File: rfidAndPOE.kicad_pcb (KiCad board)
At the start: 2 copper layers, 100 x 50 mm, 126 parts, among them J1 0813-1X1T-57-F, J2 SWD, J3 MCU Port B, J4 MCU Port C, P1 PoE-, P2 PoE+, P3 GND, P4 +5V, P5 +12V, P6 +3V3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

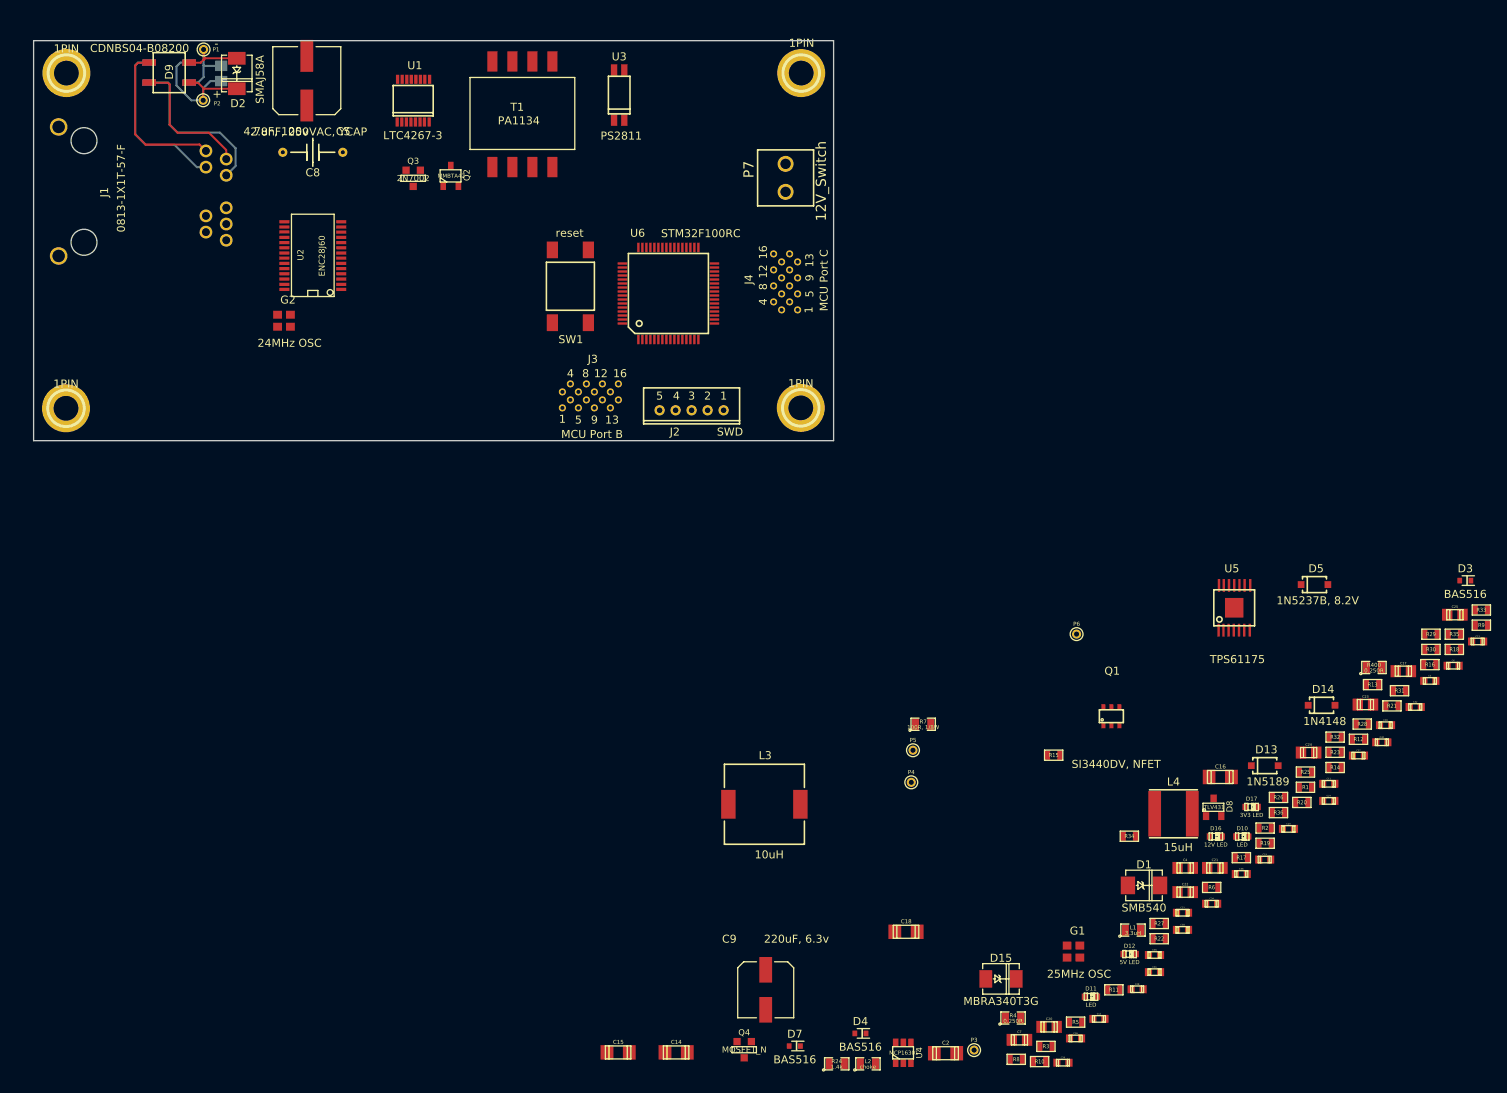
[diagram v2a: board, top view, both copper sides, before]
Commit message: Bumped up to 4 layers and changed the design rules.
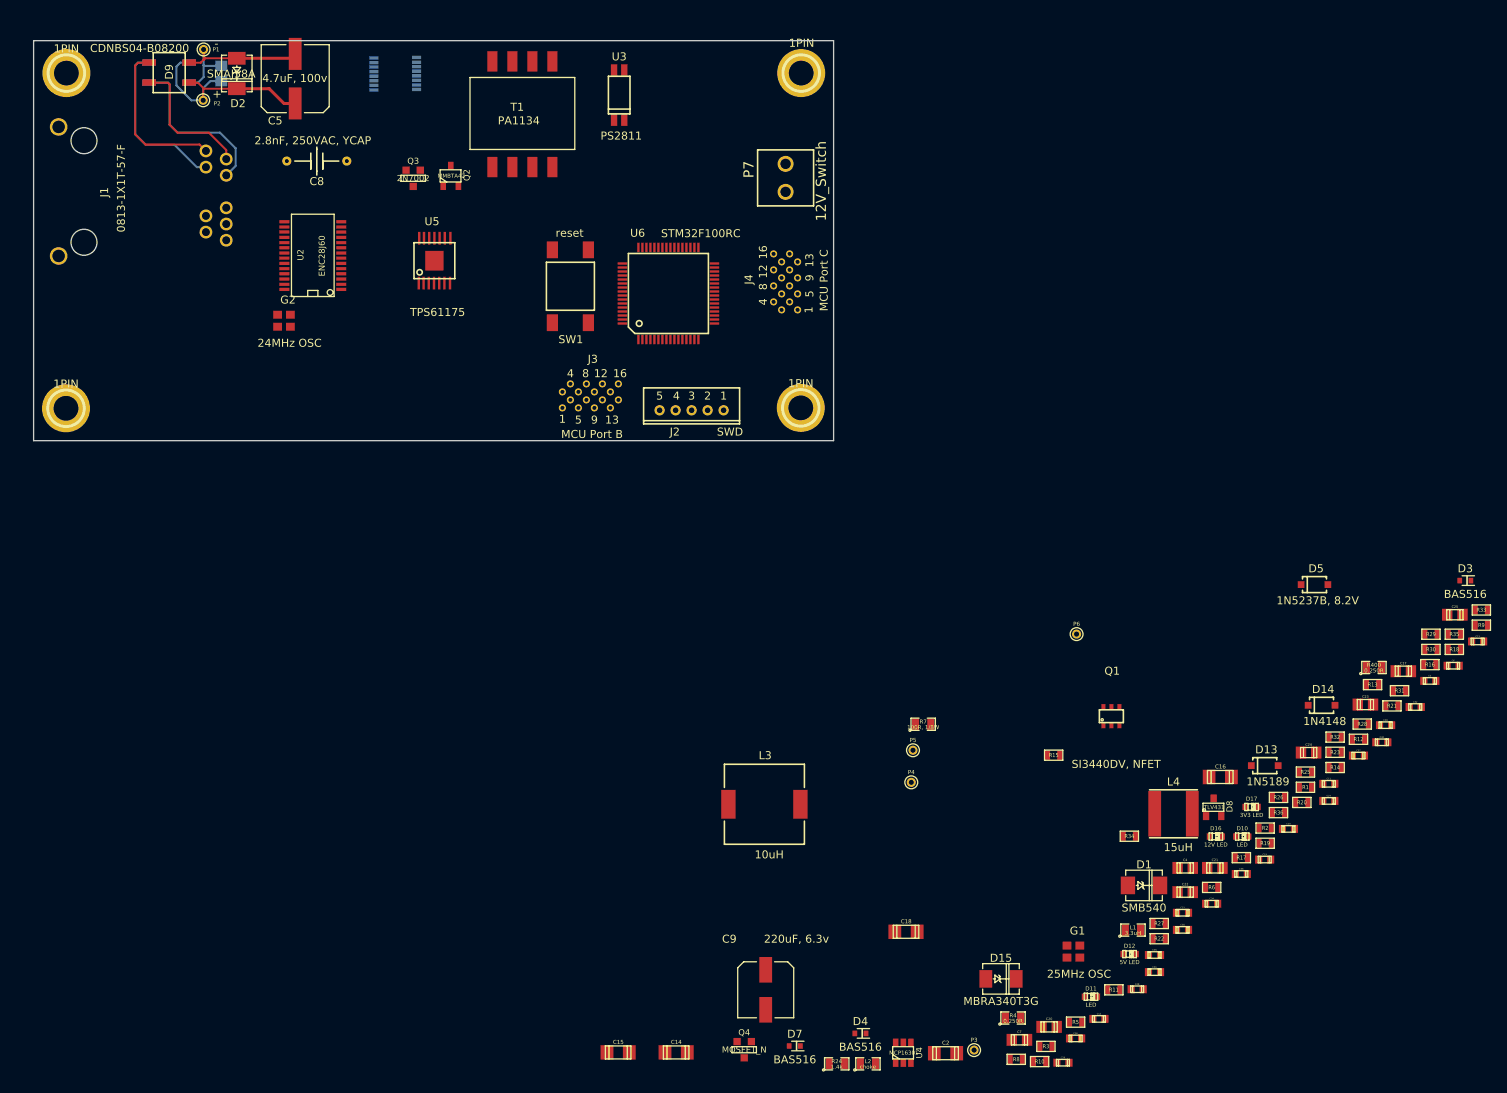
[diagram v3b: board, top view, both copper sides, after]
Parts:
- U1: moved to B.Cu
- moved U5 109.0 mm to (127.9, 58.2)
- moved U1 4.04 mm to (123.0, 34.9), turned to 90 degrees
- moved C5 1.47 mm to (110.5, 35.5)
- moved C8 1.21 mm to (113.2, 45.8)
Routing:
- net Net-(C1-Pad1): track 20.2 -> 28.3 mm
- net Net-(C1-Pad2): track 15.2 -> 22.8 mm
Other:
- copper layers 2 -> 4
- net class Default: clearance 0.254 -> 0.2; trace_width 0.254 -> 0.25
- rule trace_clearance: 0.254 -> 0.2
- rule trace_min: 0.254 -> 0.15
- rule via_min_drill: 0.508 -> 0.3
- rule via_min_size: 0.889 -> 0.45
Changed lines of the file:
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@@
     (thickness 1.6)
     (drawings 4)
-    (tracks 55)
+    (tracks 60)
     (zones 0)
     (modules 126)
@@
   (layers
     (0 F.Cu signal)
+    (1 In1.Cu signal)
+    (2 In2.Cu signal)
     (31 B.Cu signal)
     (32 B.Adhes user)
@@
     (44 Edge.Cuts user)
     (45 Margin user)
-    (46 B.CrtYd user)
-    (47 F.CrtYd user)
-    (48 B.Fab user)
-    (49 F.Fab user)
   )
   (setup
-    (last_trace_width 0.254)
-    (trace_clearance 0.254)
+    (last_trace_width 0.381)
+    (user_trace_width 0.15)
+    (user_trace_width 0.2)
+    (user_trace_width 0.25)
+    (user_trace_width 0.3)
+    (user_trace_width 0.35)
+    (user_trace_width 0.4)
+    (user_trace_width 0.45)
+    (user_trace_width 0.5)
+    (trace_clearance 0.2)
     (zone_clearance 0.508)
     (zone_45_only no)
-    (trace_min 0.254)
+    (trace_min 0.15)
     (segment_width 0.2)
     (edge_width 0.1)
     (via_size 0.889)
     (via_drill 0.635)
-    (via_min_size 0.889)
-    (via_min_drill 0.508)
+    (via_min_size 0.45)
+    (via_min_drill 0.3)
     (uvia_size 0.508)
     (uvia_drill 0.127)
@@
   (net 123 "Net-(U6-Pad50)")
   (net_class Default "This is the default net class."
-    (clearance 0.254)
-    (trace_width 0.254)
+    (clearance 0.2)
+    (trace_width 0.25)
     (via_dia 0.889)
     (via_drill 0.635)
@@
   )
   (module rfid:EEE-2AA4R7UP (layer F.Cu)
-    (at 111.95 35.7 180)
-    (fp_text reference C5 (at -4.55 -6.35 180) (layer F.SilkS)
+    (at 110.5 35.45 180)
+    (fp_text reference C5 (at 2.5 -5.25 180) (layer F.SilkS)
       (effects (font (size 1 1) (thickness 0.15)))
     )
-    (fp_text value "4.7uF, 100v" (at 3.85 -6.35 180) (layer F.SilkS)
+    (fp_text value "4.7uF, 100v" (at 0.05 0.05 180) (layer F.SilkS)
       (effects (font (size 1 1) (thickness 0.15)))
     )
@@
   )
   (module rfid:kemet_C900 (layer F.Cu)
-    (at 112.7 44.65 180)
+    (at 113.2 45.75 180)
     (fp_text reference C8 (at 0 -2.54 180) (layer F.SilkS)
       (effects (font (size 1 1) (thickness 0.15)))
@@
       (effects (font (size 1.00076 1.00076) (thickness 0.11938)))
     )
-    (fp_text value SMAJ58A (at 0.75 -2.9 270) (layer F.SilkS)
+    (fp_text value SMAJ58A (at 0.05 0.7 360) (layer F.SilkS)
       (effects (font (size 1.00076 1.00076) (thickness 0.11938)))
     )
@@
       (net 11 GND))
   )
-  (module rfid:SSOP-16 (layer F.Cu)
-    (at 125.25 38.2)
-    (fp_text reference U1 (at 0.2 -4.4) (layer F.SilkS)
-      (effects (font (size 1 1) (thickness 0.15)))
+  (module rfid:SSOP-16 (layer B.Cu)
+    (at 123 34.85 90)
+    (fp_text reference U1 (at 0.2 4.4 90) (layer B.SilkS)
+      (effects (font (size 1 1) (thickness 0.15)) (justify mirror))
     )
-    (fp_text value LTC4267-3 (at -0.05 4.35) (layer F.SilkS)
-      (effects (font (size 1 1) (thickness 0.15)))
+    (fp_text value LTC4267-3 (at -0.05 -4.35 90) (layer B.SilkS)
+      (effects (font (size 1 1) (thickness 0.15)) (justify mirror))
     )
-    (fp_line (start -2.5 1.5) (end 2.5 1.5) (layer F.SilkS) (width 0.2))
-    (fp_line (start -2.5 -1.9) (end -2.5 -1.85) (layer F.SilkS) (width 0.2))
-    (fp_line (start 2.5 -1.9) (end -2.5 -1.9) (layer F.SilkS) (width 0.2))
-    (fp_line (start 2.5 1.9) (end 2.5 -1.9) (layer F.SilkS) (width 0.2))
-    (fp_line (start -2.5 1.9) (end 2.5 1.9) (layer F.SilkS) (width 0.2))
-    (fp_line (start -2.5 -1.9) (end -2.5 1.9) (layer F.SilkS) (width 0.2))
-    (pad 4 smd rect (at -0.285716 2.667 90) (size 1.143 0.4191) (layers F.Cu F.Paste F.Mask)
+    (fp_line (start -2.5 -1.5) (end 2.5 -1.5) (layer B.SilkS) (width 0.2))
+    (fp_line (start -2.5 1.9) (end -2.5 1.85) (layer B.SilkS) (width 0.2))
+    (fp_line (start 2.5 1.9) (end -2.5 1.9) (layer B.SilkS) (width 0.2))
+    (fp_line (start 2.5 -1.9) (end 2.5 1.9) (layer B.SilkS) (width 0.2))
+    (fp_line (start -2.5 -1.9) (end 2.5 -1.9) (layer B.SilkS) (width 0.2))
+    (fp_line (start -2.5 1.9) (end -2.5 -1.9) (layer B.SilkS) (width 0.2))
+    (pad 4 smd rect (at -0.285716 -2.667) (size 1.143 0.4191) (layers B.Cu B.Paste B.Mask)
       (net 6 /PVcc))
-    (pad 3 smd rect (at -0.857144 2.667 90) (size 1.143 0.4191) (layers F.Cu F.Paste F.Mask)
+    (pad 3 smd rect (at -0.857144 -2.667) (size 1.143 0.4191) (layers B.Cu B.Paste B.Mask)
       (net 88 "Net-(Q1-Pad3)"))
-    (pad 2 smd rect (at -1.428572 2.667 90) (size 1.143 0.4191) (layers F.Cu F.Paste F.Mask)
+    (pad 2 smd rect (at -1.428572 -2.667) (size 1.143 0.4191) (layers B.Cu B.Paste B.Mask)
       (net 31 "Net-(D7-Pad1)"))
-    (pad 1 smd rect (at -2 2.667 90) (size 1.143 0.4191) (layers F.Cu F.Paste F.Mask)
+    (pad 1 smd rect (at -2 -2.667) (size 1.143 0.4191) (layers B.Cu B.Paste B.Mask)
       (net 4 GNDA))
-    (pad 8 smd rect (at 2 2.667 90) (size 1.143 0.4191) (layers F.Cu F.Paste F.Mask)
+    (pad 8 smd rect (at 2 -2.667) (size 1.143 0.4191) (layers B.Cu B.Paste B.Mask)
       (net 4 GNDA))
-    (pad 7 smd rect (at 1.4 2.667 90) (size 1.143 0.4191) (layers F.Cu F.Paste F.Mask)
+    (pad 7 smd rect (at 1.4 -2.667) (size 1.143 0.4191) (layers B.Cu B.Paste B.Mask)
       (net 2 "Net-(C1-Pad2)"))
-    (pad 6 smd rect (at 0.85714 2.667 90) (size 1.143 0.4191) (layers F.Cu F.Paste F.Mask)
+    (pad 6 smd rect (at 0.85714 -2.667) (size 1.143 0.4191) (layers B.Cu B.Paste B.Mask)
       (net 102 "Net-(U1-Pad6)"))
-    (pad 5 smd rect (at 0.285712 2.667 90) (size 1.143 0.4191) (layers F.Cu F.Paste F.Mask)
+    (pad 5 smd rect (at 0.285712 -2.667) (size 1.143 0.4191) (layers B.Cu B.Paste B.Mask)
       (net 103 "Net-(U1-Pad5)"))
-    (pad 11 smd rect (at 0.90714 -2.67 90) (size 1.143 0.4191) (layers F.Cu F.Paste F.Mask)
+    (pad 11 smd rect (at 0.90714 2.67) (size 1.143 0.4191) (layers B.Cu B.Paste B.Mask)
       (net 91 "Net-(R1-Pad1)"))
-    (pad 15 smd rect (at -1.378572 -2.67 90) (size 1.143 0.4191) (layers F.Cu F.Paste F.Mask)
+    (pad 15 smd rect (at -1.378572 2.67) (size 1.143 0.4191) (layers B.Cu B.Paste B.Mask)
       (net 4 GNDA))
-    (pad 13 smd rect (at -0.235716 -2.67 90) (size 1.143 0.4191) (layers F.Cu F.Paste F.Mask)
+    (pad 13 smd rect (at -0.235716 2.67) (size 1.143 0.4191) (layers B.Cu B.Paste B.Mask)
       (net 3 "Net-(C2-Pad1)"))
-    (pad 14 smd rect (at -0.807144 -2.67 90) (size 1.143 0.4191) (layers F.Cu F.Paste F.Mask)
+    (pad 14 smd rect (at -0.807144 2.67) (size 1.143 0.4191) (layers B.Cu B.Paste B.Mask)
       (net 92 "Net-(R5-Pad1)"))
-    (pad 9 smd rect (at 2.05 -2.67 90) (size 1.143 0.4191) (layers F.Cu F.Paste F.Mask)
+    (pad 9 smd rect (at 2.05 2.67) (size 1.143 0.4191) (layers B.Cu B.Paste B.Mask)
       (net 4 GNDA))
-    (pad 10 smd rect (at 1.45 -2.67 90) (size 1.143 0.4191) (layers F.Cu F.Paste F.Mask)
+    (pad 10 smd rect (at 1.45 2.67) (size 1.143 0.4191) (layers B.Cu B.Paste B.Mask)
       (net 4 GNDA))
-    (pad 12 smd rect (at 0.335712 -2.67 90) (size 1.143 0.4191) (layers F.Cu F.Paste F.Mask)
+    (pad 12 smd rect (at 0.335712 2.67) (size 1.143 0.4191) (layers B.Cu B.Paste B.Mask)
       (net 2 "Net-(C1-Pad2)"))
-    (pad 16 smd rect (at -1.95 -2.67 90) (size 1.143 0.4191) (layers F.Cu F.Paste F.Mask)
+    (pad 16 smd rect (at -1.95 2.67) (size 1.143 0.4191) (layers B.Cu B.Paste B.Mask)
       (net 4 GNDA))
   )
@@
   )
   (module rfid:HTSSOP-14-1EP (layer F.Cu)
-    (at 227.877095 101.589)
+    (at 127.9 58.2)
     (fp_text reference U5 (at -0.3 -4.9) (layer F.SilkS)
       (effects (font (size 1 1) (thickness 0.15)))
@@
   (gr_line (start 77.8 80.7) (end 177.8 80.7) (angle 90) (layer Edge.Cuts) (width 0.1))
   (gr_line (start 77.8 30.7) (end 77.8 80.7) (angle 90) (layer Edge.Cuts) (width 0.1))
+  (segment (start 107.24992 36.69992) (end 109.1 38.55) (width 0.381) (layer F.Cu) (net 1))
+  (segment (start 109.1 38.55) (end 110.5 38.55) (width 0.381) (layer F.Cu) (net 1))
+  (segment (start 103.2 36.69992) (end 107.24992 36.69992) (width 0.381) (layer F.Cu) (net 1))
   (segment (start 99 36.596) (end 99.10392 36.69992) (width 0.254) (layer F.Cu) (net 1))
   (segment (start 99.10392 36.69992) (end 103.2 36.69992) (width 0.254) (layer F.Cu) (net 1))
@@
   (segment (start 97.25 33.45) (end 96.146 33.45) (width 0.254) (layer B.Cu) (net 1))
   (segment (start 96.146 33.45) (end 95.65 33.946) (width 0.254) (layer B.Cu) (net 1))
+  (segment (start 103.2 32.90008) (end 109.94992 32.90008) (width 0.381) (layer F.Cu) (net 2))
+  (segment (start 109.94992 32.90008) (end 110.5 32.35) (width 0.381) (layer F.Cu) (net 2))
   (segment (start 99.05 33.1) (end 99.24992 32.90008) (width 0.254) (layer F.Cu) (net 2))
   (segment (start 99.24992 32.90008) (end 103.2 32.90008) (width 0.254) (layer F.Cu) (net 2))

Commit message: Got some of the ethernet routing in place (50 ohm terminators, en28j60). Moved a bunch of the flyback circuitry in place and routed some of it.
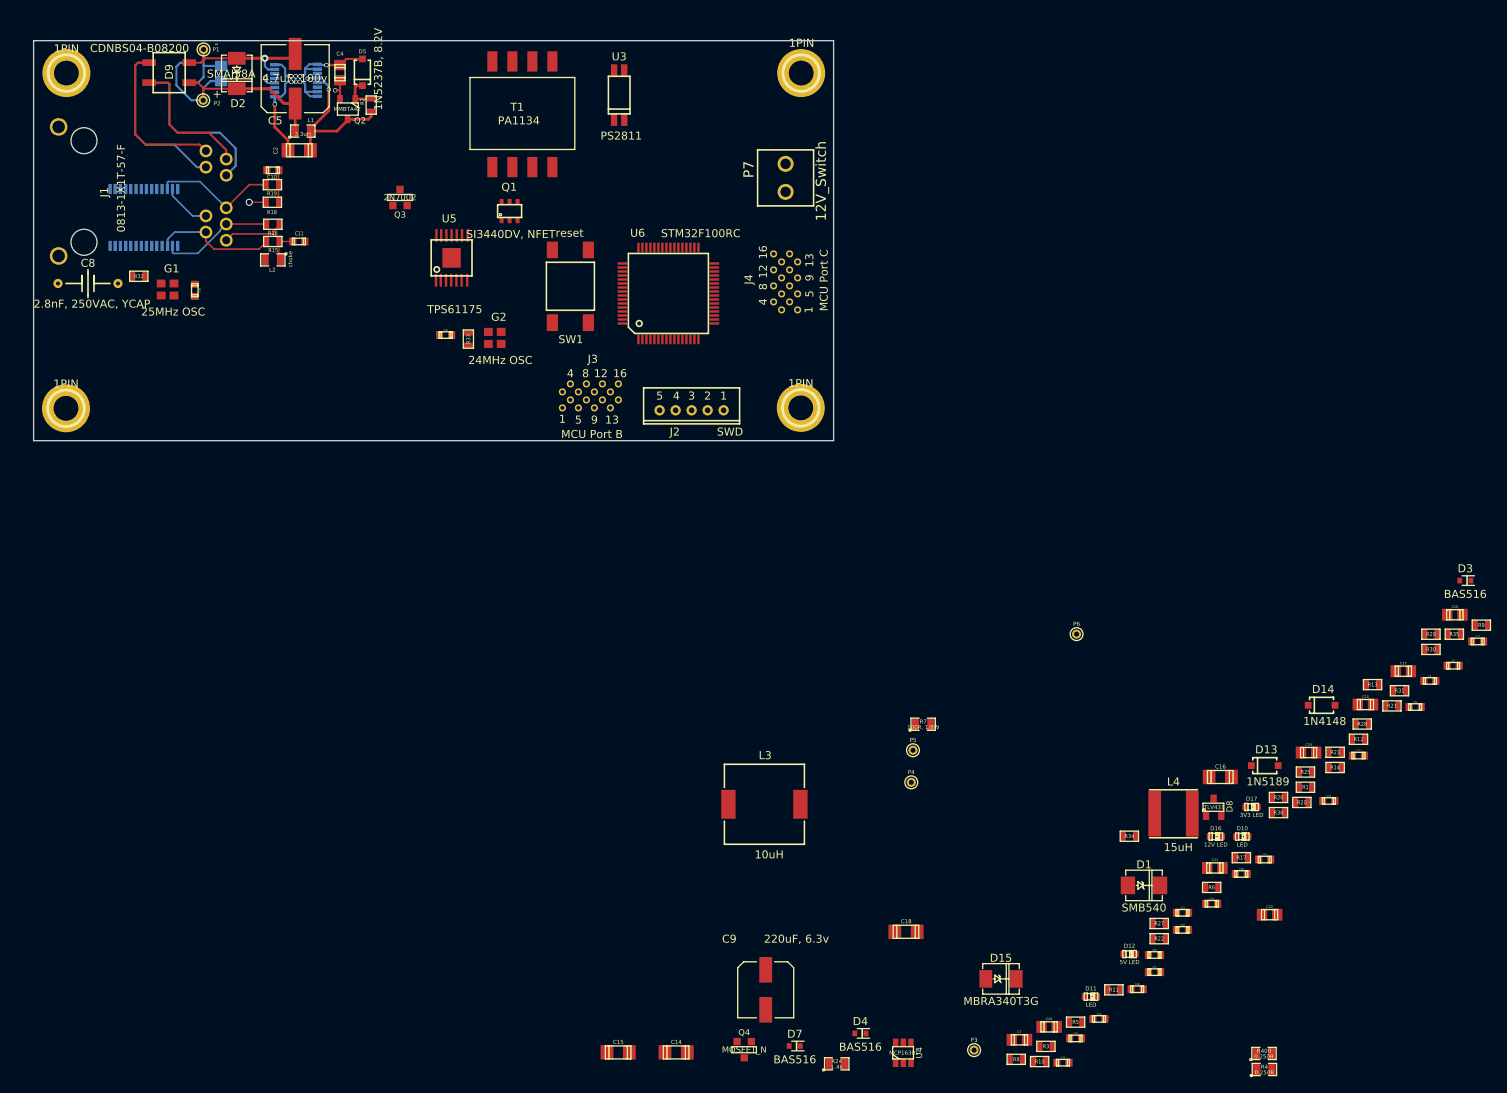
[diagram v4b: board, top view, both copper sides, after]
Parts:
- U2: moved to B.Cu
- moved R32 160.3 mm to (91.0, 60.1), turned to 180 degrees
- moved C30 158.8 mm to (98.0, 61.9), turned to 270 degrees
- moved R18 158.0 mm to (107.7, 50.9), turned to 180 degrees
- moved R16 154.8 mm to (107.7, 53.6), turned to 180 degrees
- moved C10 151.3 mm to (107.7, 46.9)
- moved R19 148.9 mm to (107.7, 48.7), turned to 180 degrees
- moved C11 145.5 mm to (111.0, 55.8), turned to 180 degrees
- moved C4 145.1 mm to (116.1, 34.7), turned to 90 degrees
- moved L1 144.0 mm to (111.5, 42.0)
- moved R2 143.7 mm to (120.0, 38.8), turned to 90 degrees
- moved G1 140.3 mm to (94.5, 61.8)
- moved C2 138.8 mm to (111.0, 44.4)
- moved D5 135.1 mm to (118.9, 34.6), turned to 90 degrees
- moved R33 131.1 mm to (132.2, 68.0), turned to 270 degrees
- moved C39 127.2 mm to (129.3, 67.5)
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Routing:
- net GNDA: track 0.00 -> 34.0 mm, vias 0 -> 8
- net Net-(C2-Pad1): track 0.00 -> 19.7 mm, vias 0 -> 1
- net /TPIN+: track 0.00 -> 16.6 mm, vias 0 -> 1
- net /TPIN-: track 0.00 -> 15.8 mm
- net /TPOUT+: track 0.00 -> 15.5 mm
- net /PVcc: track 0.00 -> 14.7 mm, vias 0 -> 2
- net /TPOUT-: track 0.00 -> 14.2 mm
- net Net-(C11-Pad1): track 0.00 -> 13.1 mm
- net Net-(C1-Pad2): track 22.8 -> 33.0 mm, vias 0 -> 2
- net Net-(D5-Pad2): track 0.00 -> 4.48 mm
- net Net-(C10-Pad1): track 0.00 -> 4.02 mm
- net Net-(C1-Pad1): track 28.3 -> 31.7 mm
- added copper zone on In2.Cu, net GNDA
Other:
- net class Default: via_dia 0.889 -> 0.55; via_drill 0.635 -> 0.4

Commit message: Moved the flyback transformer in to place as well as the switching transistor and supporting circuitry for that. Routed traces to them. Just the power good/feedback circuit left to place and route on the isolated side.
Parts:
- Q1, R4, R400, R5: moved to B.Cu
- moved R4 168.9 mm to (117.8, 34.5), turned to 180 degrees
- moved R400 165.7 mm to (117.8, 36.9), turned to 180 degrees
- moved C3 151.3 mm to (121.6, 34.6), turned to 180 degrees
- moved D3 147.3 mm to (119.2, 45.5), turned to 180 degrees
- moved R5 145.6 mm to (118.0, 39.0)
- moved R3 145.5 mm to (114.9, 41.6), turned to 90 degrees
- moved R6 141.0 mm to (119.2, 43.5)
- moved R7 103.4 mm to (123.3, 36.4)
- moved Q1 23.2 mm to (122.0, 34.5), turned to 270 degrees
- moved U3 19.8 mm to (134.9, 49.1), turned to 90 degrees
- moved T1 15.0 mm to (127.0, 33.9), turned to 270 degrees
- moved Q3 4.02 mm to (119.6, 50.6)
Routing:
- net Net-(Q1-Pad3): track 0.00 -> 21.6 mm, vias 0 -> 2
- net Net-(C2-Pad1): track 19.7 -> 34.2 mm
- net GNDA: track 34.0 -> 41.8 mm
- net Net-(Q1-Pad4): track 0.00 -> 6.36 mm
- net Net-(Q1-Pad1): track 0.00 -> 5.82 mm, vias 0 -> 3
- net Net-(R5-Pad1): track 0.00 -> 5.26 mm
- net Net-(C3-Pad2): track 0.00 -> 1.75 mm
- added copper zone on B.Cu, net Net-(Q1-Pad1)
